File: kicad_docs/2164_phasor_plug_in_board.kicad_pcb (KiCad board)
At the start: 2 copper layers, 58.4 x 50.8 mm, 85 parts, among them J1 Conn_01x04_Male, J2 Conn_01x04_Male, J3 Conn_01x04_Male, J4 Conn_01x08_Male, U1 TL074, U2 SSM2164, U3 TL074, U4 SSM2164, U5 TL074, U6 TL072

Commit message: add github url to board, add pic of board bottom
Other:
- board text added: "github.com/JordanAceto/2164_phasor_plug_in_board rev1 2019-06-11"
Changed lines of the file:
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@@
   (general
     (thickness 1.6)
-    (drawings 13)
+    (drawings 14)
     (tracks 837)
     (zones 0)
@@
     )
   )
+  (gr_text "github.com/JordanAceto/2164_phasor_plug_in_board\nrev1\n2019-06-11" (at 151.13 54.61) (layer B.SilkS)
+    (effects (font (size 1 1) (thickness 0.15)) (justify left mirror))
+  )
   (gr_circle (center 105.977961 67.31) (end 105.918 66.802) (layer F.SilkS) (width 0.15))

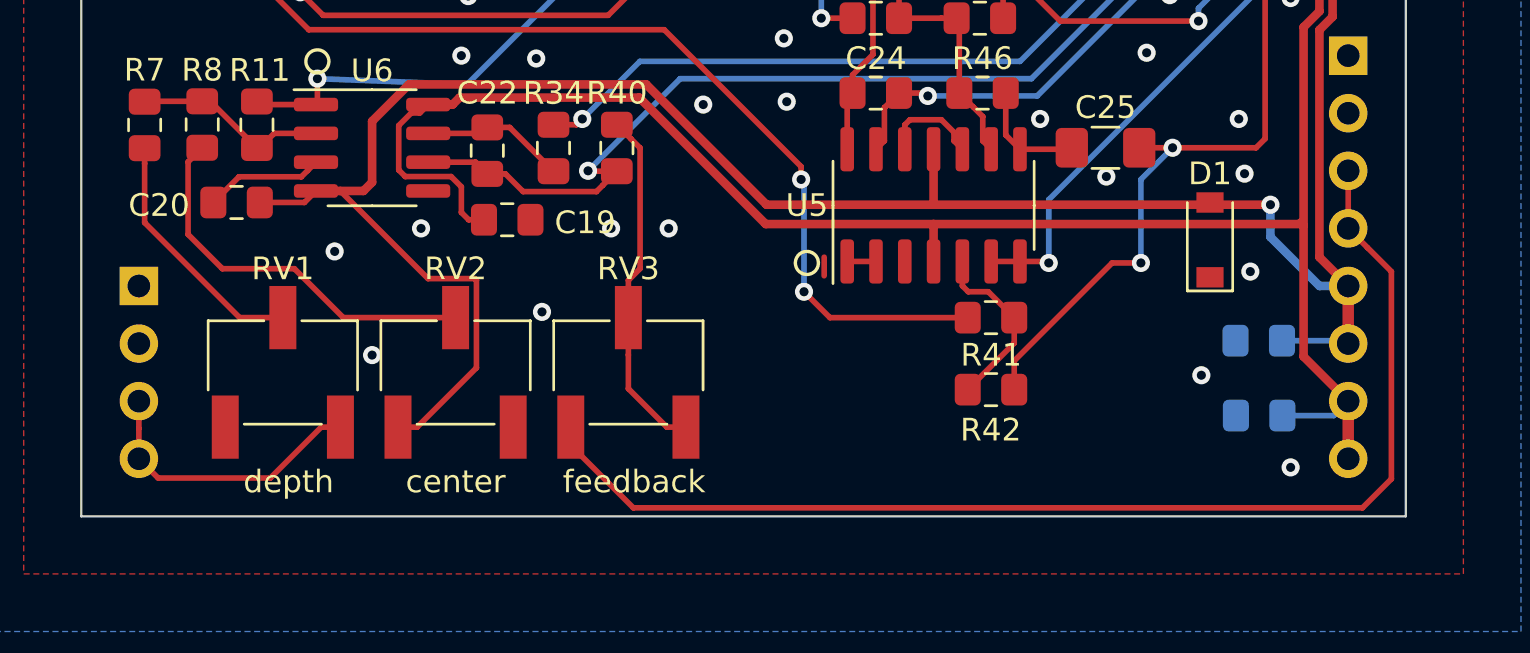
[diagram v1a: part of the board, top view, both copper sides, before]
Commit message: change trimmers to cheaper TH type
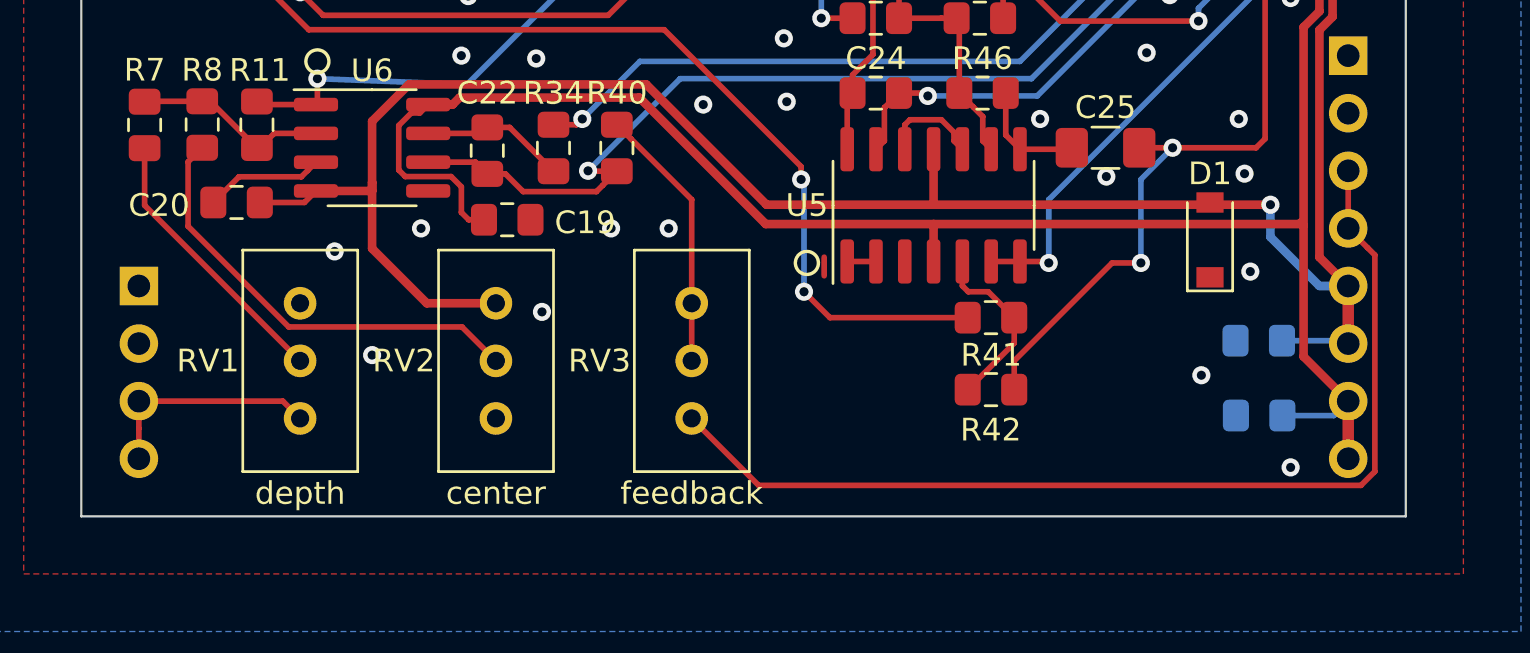
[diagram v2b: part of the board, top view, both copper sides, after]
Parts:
- RV1, RV2, RV3: footprint Potentiometer_SMD:Potentiometer_Bourns_3269W_Vertical -> Potentiometer_THT:Potentiometer_Bourns_3296W_Vertical
- moved RV3 4.13 mm to (128.5, 92.2), turned to 90 degrees
- moved RV2 3.53 mm to (119.9, 92.2), turned to 90 degrees
- moved RV1 3.14 mm to (111.3, 92.2), turned to 90 degrees
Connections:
- RV3 pad 1: Net-(J4-Pad3) -> Net-(R40-Pad2)
- RV3 pad 3: Net-(R40-Pad2) -> Net-(J4-Pad3)
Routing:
- net Net-(J4-Pad3): track 53.0 -> 45.4 mm
- net -12V: track 176.4 -> 170.0 mm
- net Net-(R40-Pad2): track 15.5 -> 11.8 mm
- net Net-(J1-Pad3): track 12.7 -> 9.97 mm
- net Net-(R8-Pad2): track 17.4 -> 19.8 mm
- net Net-(R7-Pad2): track 11.1 -> 12.2 mm
